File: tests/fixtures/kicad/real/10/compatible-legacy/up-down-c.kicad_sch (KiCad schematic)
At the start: 1 part

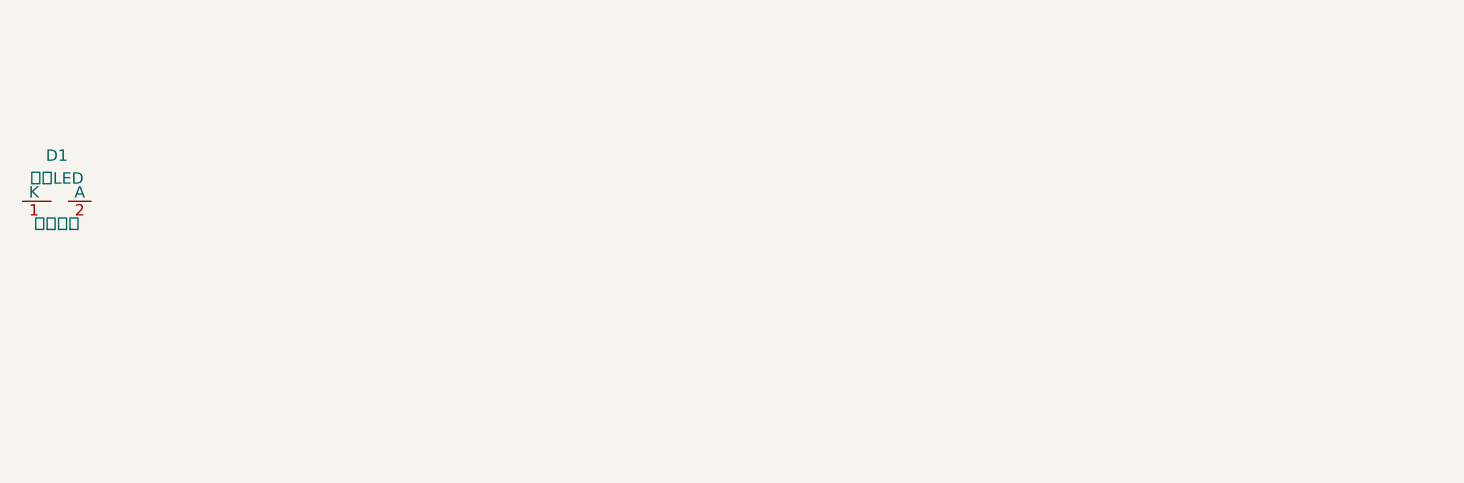
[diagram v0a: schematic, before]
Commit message: fix: validate real KiCad 10 reports and fixtures
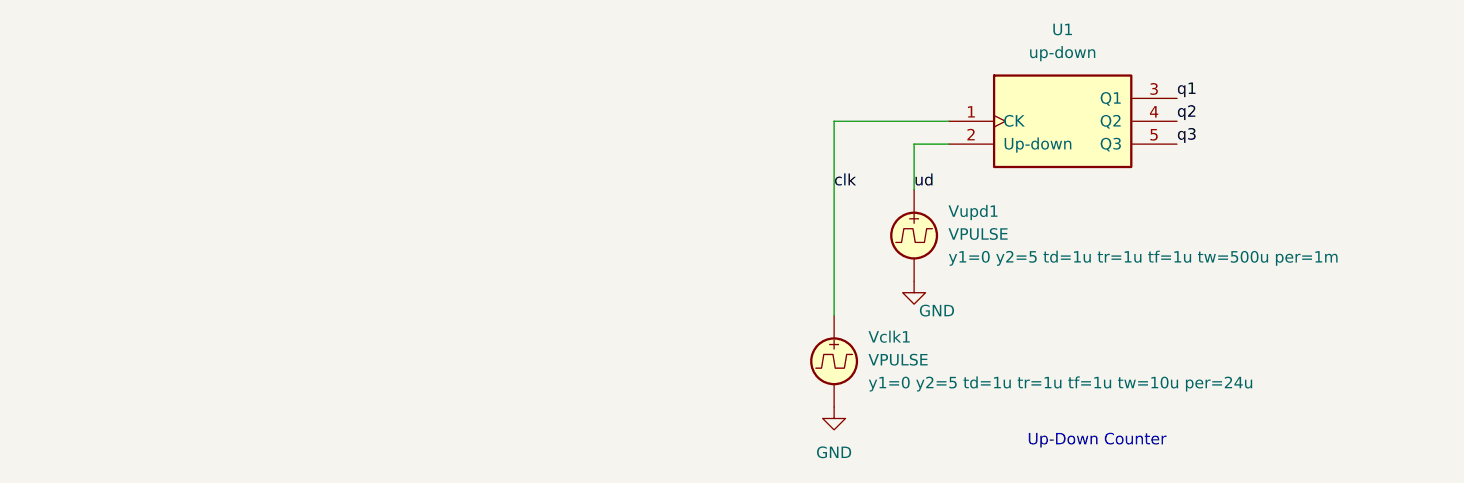
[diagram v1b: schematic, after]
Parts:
- removed D1: 状态LED, LED_THT:LED_D5.0mm, symbol Device:LED
- added U1: up-down, symbol up-down:Up-Down
- added Vclk1, Vupd1: VPULSE, symbol Simulation_SPICE:VPULSE
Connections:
- new net GND: Vclk1.2, Vupd1.2
- new net clk: U1.1 (CK), Vclk1.1
- new net q1: U1.3 (Q1)
- new net q2: U1.4 (Q2)
- new net q3: U1.5 (Q3)
- new net ud: U1.2 (Up-down), Vupd1.1
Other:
- note added: "Up-Down Counter"
